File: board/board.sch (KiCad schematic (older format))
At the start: 12 parts, among them J1 MOTION DETECTOR, J2 EXT BUTTON, U1 APA102 (RGB), U2 APA102 (W)

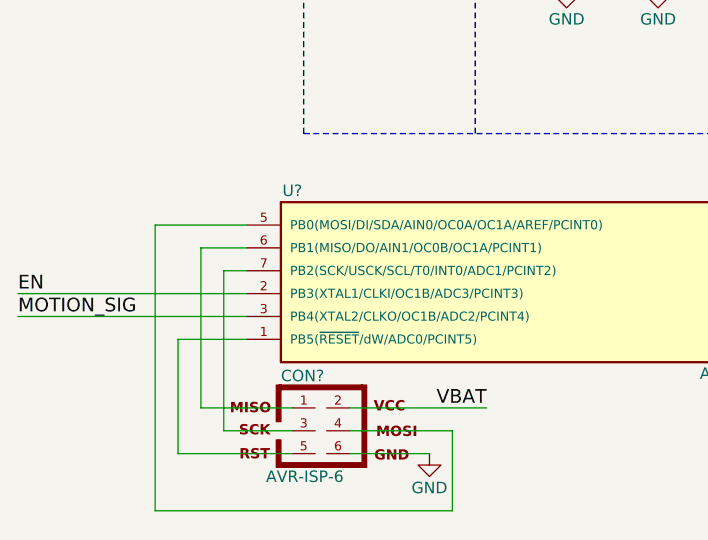
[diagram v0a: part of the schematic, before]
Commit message: Add attiny85 to control power
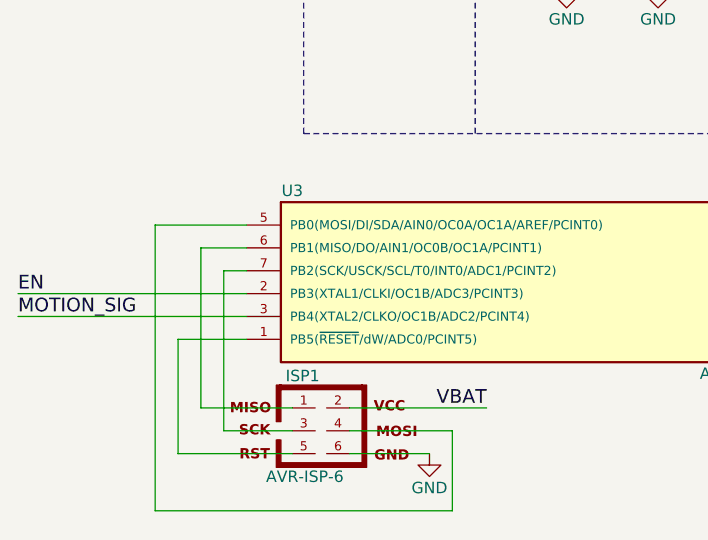
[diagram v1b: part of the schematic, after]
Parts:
- ISP1: renamed from CON?; footprint AVR-ISP-6 -> Pin_Headers:Pin_Header_Straight_2x03_Pitch2.54mm
- J1: footprint Pin_Headers:Pin_Header_Straight_1x03_Pitch2.54mm -> Pin_Headers:Pin_Header_Angled_1x03_Pitch2.54mm
- J2: footprint Pin_Headers:Pin_Header_Straight_1x02_Pitch2.54mm -> Pin_Headers:Pin_Header_Angled_1x02_Pitch2.54mm
- R1, R2, R4: footprint Discret:R3 -> Resistors_SMD:R_0805_HandSoldering
- U3: renamed from U?; footprint Housings_DIP:DIP-8_W7.62mm -> Housings_SOIC:SOIC-8_3.9x4.9mm_Pitch1.27mm
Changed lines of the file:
@@
 Adafruit FeatherWing\n
 $Comp
-L VCC #PWR8
+L VCC #PWR01
 U 1 1 56D753B8
 P 9700 750
-F 0 "#PWR8" H 9700 600 50  0001 C CNN
+F 0 "#PWR01" H 9700 600 50  0001 C CNN
 F 1 "VCC" H 9700 900 50  0000 C CNN
 F 2 "" H 9700 750 50  0000 C CNN
@@
 $EndComp
 $Comp
-L GND #PWR9
+L GND #PWR02
 U 1 1 56D75A03
 P 9700 2500
-F 0 "#PWR9" H 9700 2250 50  0001 C CNN
+F 0 "#PWR02" H 9700 2250 50  0001 C CNN
 F 1 "GND" H 9700 2350 50  0000 C CNN
 F 2 "" H 9700 2500 50  0000 C CNN
@@
 NoConn ~ 10050 2400
 $Comp
-L GND #PWR6
+L GND #PWR03
 U 1 1 59796D2F
 P 7800 3800
-F 0 "#PWR6" H 7800 3550 50  0001 C CNN
+F 0 "#PWR03" H 7800 3550 50  0001 C CNN
 F 1 "GND" H 7800 3650 50  0000 C CNN
 F 2 "" H 7800 3800 50  0001 C CNN
@@
 F 0 "J1" H 7400 1150 50  0000 C CNN
 F 1 "MOTION DETECTOR" V 7500 950 50  0000 C CNN
-F 2 "Pin_Headers:Pin_Header_Straight_1x03_Pitch2.54mm" H 7400 950 50  0001 C CNN
+F 2 "Pin_Headers:Pin_Header_Angled_1x03_Pitch2.54mm" H 7400 950 50  0001 C CNN
 F 3 "" H 7400 950 50  0001 C CNN
 	1    7400 950
@@
 F 0 "R1" V 5700 1200 50  0000 C CNN
 F 1 "22.6K" V 5800 1200 39  0000 C CNN
-F 2 "Discret:R3" V 5730 1200 50  0001 C CNN
+F 2 "Resistors_SMD:R_0805_HandSoldering" V 5730 1200 50  0001 C CNN
 F 3 "" H 5800 1200 50  0001 C CNN
 	1    5800 1200
@@
 F 0 "R2" V 5880 1950 50  0000 C CNN
 F 1 "10K" V 5800 1950 50  0000 C CNN
-F 2 "Discret:R3" V 5730 1950 50  0001 C CNN
+F 2 "Resistors_SMD:R_0805_HandSoldering" V 5730 1950 50  0001 C CNN
 F 3 "" H 5800 1950 50  0001 C CNN
 	1    5800 1950
@@
 Connection ~ 5800 1400
 $Comp
-L GND #PWR3
+L GND #PWR04
 U 1 1 597CE63C
 P 5800 2100
-F 0 "#PWR3" H 5800 1850 50  0001 C CNN
+F 0 "#PWR04" H 5800 1850 50  0001 C CNN
 F 1 "GND" H 5800 1950 50  0000 C CNN
 F 2 "" H 5800 2100 50  0001 C CNN
@@
 $EndComp
 $Comp
-L VCC #PWR2
+L VCC #PWR05
 U 1 1 597CEF49
 P 5800 1050
-F 0 "#PWR2" H 5800 900 50  0001 C CNN
+F 0 "#PWR05" H 5800 900 50  0001 C CNN
 F 1 "VCC" H 5800 1200 50  0000 C CNN
 F 2 "" H 5800 1050 50  0001 C CNN
@@
 F 0 "R4" V 6280 1950 50  0000 C CNN
 F 1 "10K" V 6200 1950 50  0000 C CNN
-F 2 "Discret:R3" V 6130 1950 50  0001 C CNN
+F 2 "Resistors_SMD:R_0805_HandSoldering" V 6130 1950 50  0001 C CNN
 F 3 "" H 6200 1950 50  0001 C CNN
 	1    6200 1950
@@
 $EndComp
 $Comp
-L GND #PWR4
+L GND #PWR06
 U 1 1 597D0A0F
 P 6200 2100
-F 0 "#PWR4" H 6200 1850 50  0001 C CNN
+F 0 "#PWR06" H 6200 1850 50  0001 C CNN
 F 1 "GND" H 6200 1950 50  0000 C CNN
 F 2 "" H 6200 2100 50  0001 C CNN
@@
 Connection ~ 6200 1750
 $Comp
-L GND #PWR7
+L GND #PWR07
 U 1 1 597D0EF3
 P 7950 2350
-F 0 "#PWR7" H 7950 2100 50  0001 C CNN
+F 0 "#PWR07" H 7950 2100 50  0001 C CNN
 F 1 "GND" H 7950 2200 50  0000 C CNN
 F 2 "" H 7950 2350 50  0001 C CNN
@@
 F 0 "J2" H 5000 1650 50  0000 C CNN
 F 1 "EXT BUTTON" V 5100 1500 50  0000 C CNN
-F 2 "Pin_Headers:Pin_Header_Straight_1x02_Pitch2.54mm" H 5000 1500 50  0001 C CNN
+F 2 "Pin_Headers:Pin_Header_Angled_1x02_Pitch2.54mm" H 5000 1500 50  0001 C CNN
 F 3 "" H 5000 1500 50  0001 C CNN
 	1    5000 1500
@@
 $EndComp
 $Comp
-L GND #PWR1
+L GND #PWR08
 U 1 1 597D2087
 P 5050 1900
-F 0 "#PWR1" H 5050 1650 50  0001 C CNN
+F 0 "#PWR08" H 5050 1650 50  0001 C CNN
 F 1 "GND" H 5050 1750 50  0000 C CNN
 F 2 "" H 5050 1900 50  0001 C CNN
@@
 	4650 2750 4650 500
 $Comp
-L ATTINY85-20PU U?
+L ATTINY85-20PU U3
 U 1 1 597D0F49
 P 5750 3400
-F 0 "U?" H 4600 3800 50  0000 C CNN
+F 0 "U3" H 4600 3800 50  0000 C CNN
 F 1 "ATTINY85-20PU" H 6650 3000 50  0000 C CNN
-F 2 "Housings_DIP:DIP-8_W7.62mm" H 6750 3400 50  0001 C CIN
+F 2 "Housings_SOIC:SOIC-8_3.9x4.9mm_Pitch1.27mm" H 6750 3400 50  0001 C CIN
 F 3 "" H 5750 3400 50  0001 C CNN
 	1    5750 3400
@@
 $EndComp
 $Comp
-L GND #PWR?
+L GND #PWR09
 U 1 1 597D1088
 P 7100 3650
-F 0 "#PWR?" H 7100 3400 50  0001 C CNN
+F 0 "#PWR09" H 7100 3400 50  0001 C CNN
 F 1 "GND" H 7100 3500 50  0000 C CNN
 F 2 "" H 7100 3650 50  0001 C CNN
@@
 $EndComp
 $Comp
-L AVR-ISP-6 CON?
+L AVR-ISP-6 ISP1
 U 1 1 597D1114
 P 4750 4050
-F 0 "CON?" H 4645 4290 50  0000 C CNN
+F 0 "ISP1" H 4645 4290 50  0000 C CNN
 F 1 "AVR-ISP-6" H 4485 3820 50  0000 L BNN
-F 2 "AVR-ISP-6" V 4230 4090 50  0001 C CNN
+F 2 "Pin_Headers:Pin_Header_Straight_2x03_Pitch2.54mm" V 4230 4090 50  0001 C CNN
 F 3 "" H 4725 4050 50  0001 C CNN
 	1    4750 4050
@@
 	4300 3350 4400 3350
 $Comp
-L GND #PWR?
+L GND #PWR010
 U 1 1 597D12FA
 P 5200 4150
-F 0 "#PWR?" H 5200 3900 50  0001 C CNN
+F 0 "#PWR010" H 5200 3900 50  0001 C CNN
 F 1 "GND" H 5200 4000 50  0000 C CNN
 F 2 "" H 5200 4150 50  0001 C CNN
@@
 	7800 2350 7800 1750
 $Comp
-L VCC #PWR?
+L VCC #PWR011
 U 1 1 597D3E37
 P 7800 1750
-F 0 "#PWR?" H 7800 1600 50  0001 C CNN
+F 0 "#PWR011" H 7800 1600 50  0001 C CNN
 F 1 "VCC" H 7800 1900 50  0000 C CNN
 F 2 "" H 7800 1750 50  0001 C CNN

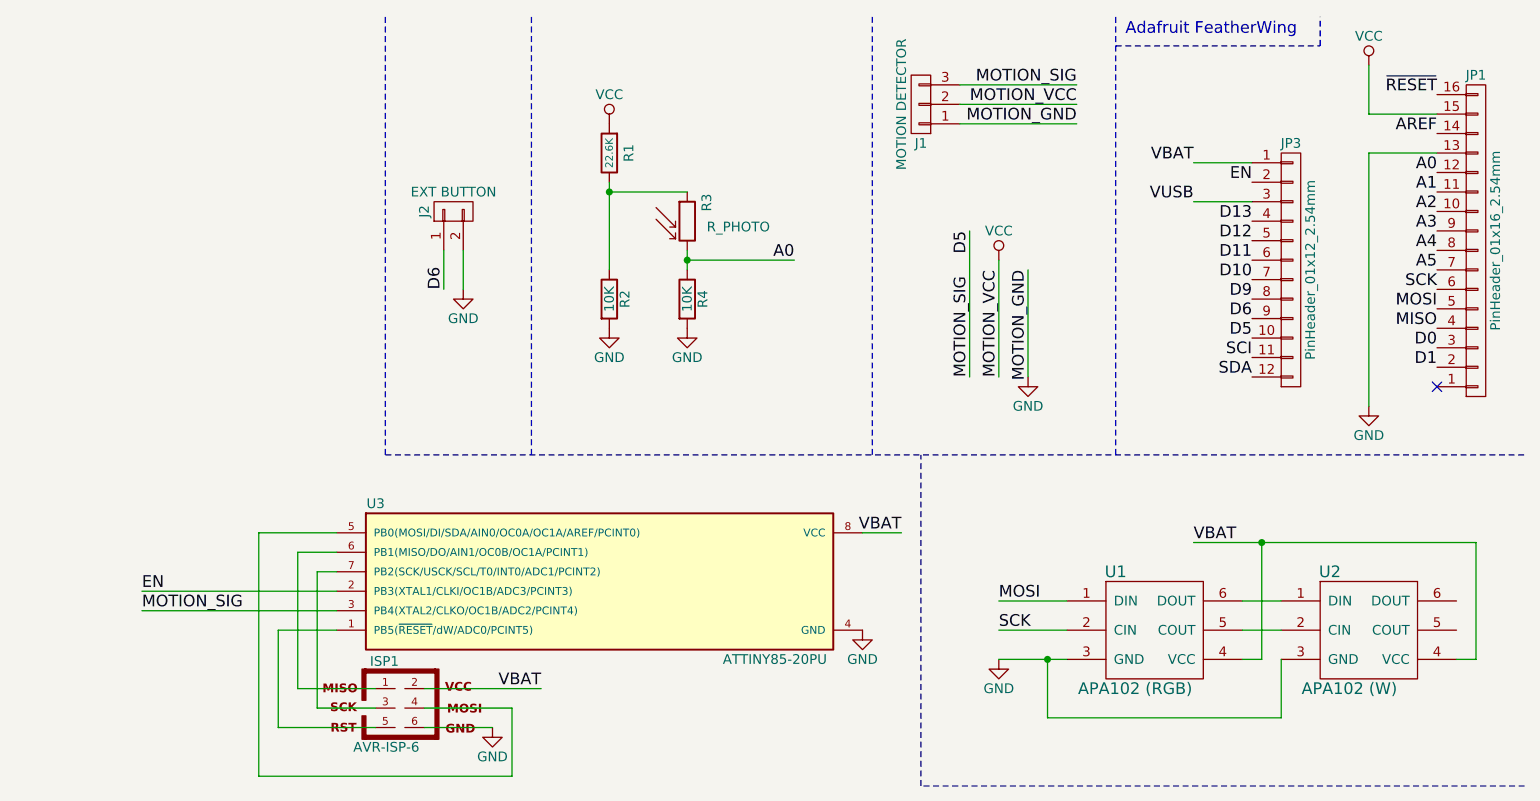
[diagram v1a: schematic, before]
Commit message: Add protection resistors
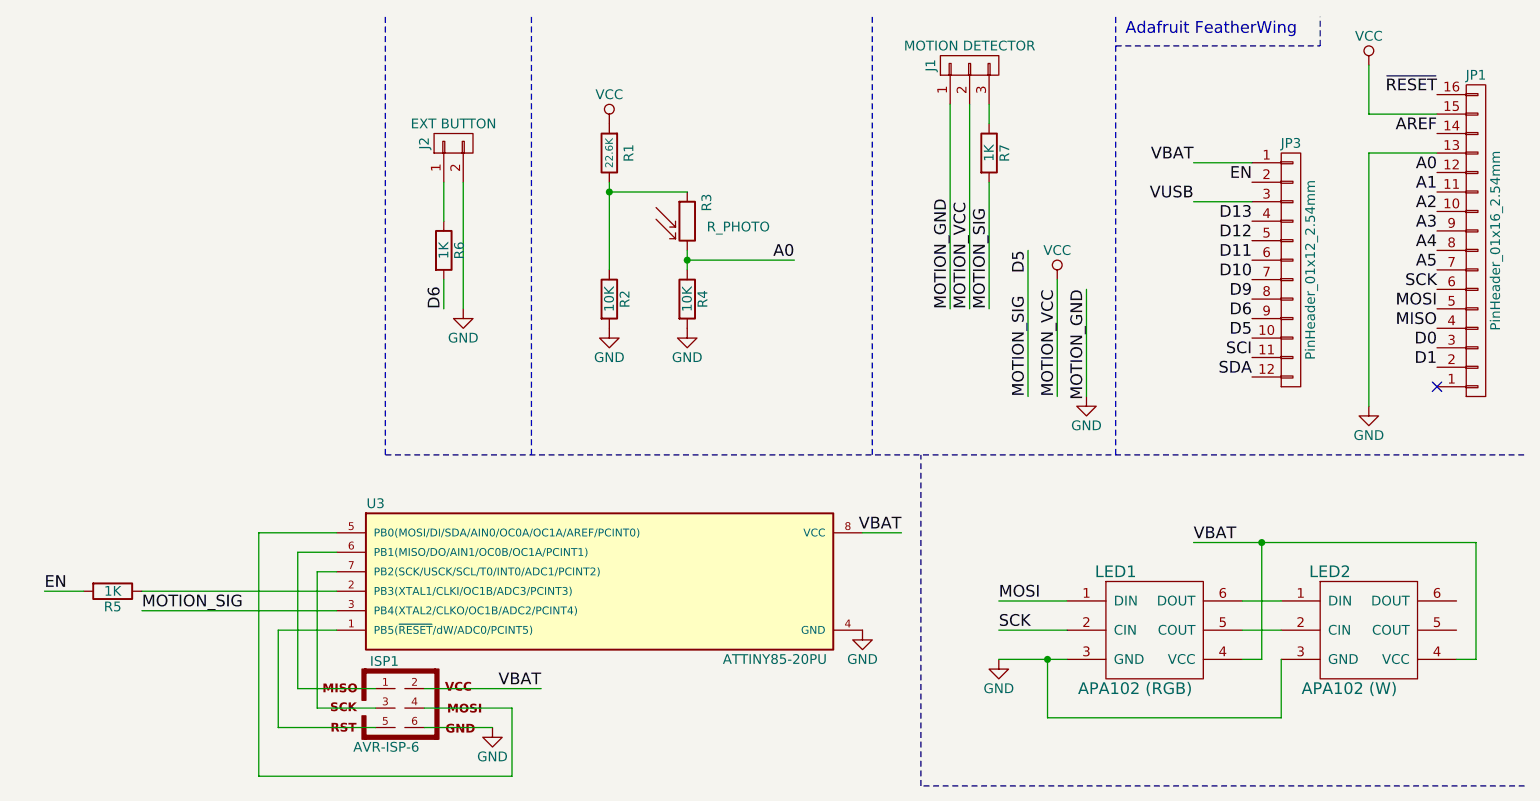
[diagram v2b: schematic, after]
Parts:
- added R5, R6, R7: 1K, Resistors_SMD:R_0805_HandSoldering, symbol R
- renumbered U1 to LED1, U2 to LED2
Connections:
- net D5: now also R7.2; no longer J1.3 (P3)
- net D6: now also R6.2; no longer J2.1 (P1)
- net EN: now also R5.2; no longer U3.2 (PB3(XTAL1/CLKI/OC1B/ADC3/PCINT3))
- new net: J1.3 (P3), R7.1
- new net: R5.1, U3.2 (PB3(XTAL1/CLKI/OC1B/ADC3/PCINT3))
- new net: J2.1 (P1), R6.1
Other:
- moved on the sheet: J1, J2
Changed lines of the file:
@@
 MOSI
 $Comp
-L APA102 U1
+L APA102 LED1
 U 1 1 59797576
 P 8600 3650
-F 0 "U1" H 8400 3950 60  0000 C CNN
+F 0 "LED1" H 8400 3950 60  0000 C CNN
 F 1 "APA102 (RGB)" H 8500 3350 60  0000 C CNN
 F 2 "CrumpPrints:APA102" H 8600 3200 60  0001 C CNN
@@
 	7800 3800 8150 3800
 $Comp
-L APA102 U2
+L APA102 LED2
 U 1 1 5979778F
 P 9700 3650
-F 0 "U2" H 9500 3950 60  0000 C CNN
+F 0 "LED2" H 9500 3950 60  0000 C CNN
 F 1 "APA102 (W)" H 9600 3350 60  0000 C CNN
 F 2 "CrumpPrints:APA102" H 9700 3200 60  0001 C CNN
@@
 L CONN_01X03 J1
 U 1 1 59797A62
-P 7400 950
-F 0 "J1" H 7400 1150 50  0000 C CNN
-F 1 "MOTION DETECTOR" V 7500 950 50  0000 C CNN
-F 2 "Pin_Headers:Pin_Header_Angled_1x03_Pitch2.54mm" H 7400 950 50  0001 C CNN
-F 3 "" H 7400 950 50  0001 C CNN
-	1    7400 950
-	-1   0    0    1
+P 7650 750
+F 0 "J1" H 7650 950 50  0000 C CNN
+F 1 "MOTION DETECTOR" V 7750 750 50  0000 C CNN
+F 2 "Pin_Headers:Pin_Header_Angled_1x03_Pitch2.54mm" H 7650 750 50  0001 C CNN
+F 3 "" H 7650 750 50  0001 C CNN
+	1    7650 750
+	0    -1   -1   0
 $EndComp
 $Comp
@@
 L GND #PWR07
 U 1 1 597D0EF3
-P 7950 2350
-F 0 "#PWR07" H 7950 2100 50  0001 C CNN
-F 1 "GND" H 7950 2200 50  0000 C CNN
-F 2 "" H 7950 2350 50  0001 C CNN
-F 3 "" H 7950 2350 50  0001 C CNN
-	1    7950 2350
-	1    0    0    -1
-$EndComp
-Wire Wire Line
-	7650 1600 7650 2350
-Text Label 7650 1600 3    60   ~ 0
+P 8250 2450
+F 0 "#PWR07" H 8250 2200 50  0001 C CNN
+F 1 "GND" H 8250 2300 50  0000 C CNN
+F 2 "" H 8250 2450 50  0001 C CNN
+F 3 "" H 8250 2450 50  0001 C CNN
+	1    8250 2450
+	1    0    0    -1
+$EndComp
+Wire Wire Line
+	7950 1700 7950 2450
+Text Label 7950 1700 3    60   ~ 0
 D5
 Wire Notes Line
@@
 L CONN_01X02 J2
 U 1 1 597D1FB0
-P 5000 1500
-F 0 "J2" H 5000 1650 50  0000 C CNN
-F 1 "EXT BUTTON" V 5100 1500 50  0000 C CNN
-F 2 "Pin_Headers:Pin_Header_Angled_1x02_Pitch2.54mm" H 5000 1500 50  0001 C CNN
-F 3 "" H 5000 1500 50  0001 C CNN
-	1    5000 1500
+P 5000 1150
+F 0 "J2" H 5000 1300 50  0000 C CNN
+F 1 "EXT BUTTON" V 5100 1150 50  0000 C CNN
+F 2 "Pin_Headers:Pin_Header_Angled_1x02_Pitch2.54mm" H 5000 1150 50  0001 C CNN
+F 3 "" H 5000 1150 50  0001 C CNN
+	1    5000 1150
 	0    -1   -1   0
 $EndComp
@@
 L GND #PWR08
 U 1 1 597D2087
-P 5050 1900
-F 0 "#PWR08" H 5050 1650 50  0001 C CNN
-F 1 "GND" H 5050 1750 50  0000 C CNN
-F 2 "" H 5050 1900 50  0001 C CNN
-F 3 "" H 5050 1900 50  0001 C CNN
-	1    5050 1900
-	1    0    0    -1
-$EndComp
-Wire Wire Line
-	5050 1700 5050 1900
-Wire Wire Line
-	4950 1700 4950 1900
-Text Label 4950 1900 1    60   ~ 0
+P 5050 2000
+F 0 "#PWR08" H 5050 1750 50  0001 C CNN
+F 1 "GND" H 5050 1850 50  0000 C CNN
+F 2 "" H 5050 2000 50  0001 C CNN
+F 3 "" H 5050 2000 50  0001 C CNN
+	1    5050 2000
+	1    0    0    -1
+$EndComp
+Wire Wire Line
+	5050 1350 5050 2000
+Wire Wire Line
+	4950 1350 4950 1550
+Text Label 4950 2000 1    60   ~ 0
 D6
 Wire Notes Line
@@
 Wire Wire Line
 	4400 3450 3400 3450
-Text Label 3400 3450 0    60   ~ 0
+Text Label 2900 3450 0    60   ~ 0
 EN
-Text Label 8200 1050 2    60   ~ 0
+Text Label 7550 2000 1    60   ~ 0
 MOTION_GND
 Wire Wire Line
-	8200 1050 7600 1050
-Wire Wire Line
-	8200 950  7600 950
-Wire Wire Line
-	8200 850  7600 850
-Text Label 8200 950  2    60   ~ 0
+	7550 2000 7550 950
+Wire Wire Line
+	7650 2000 7650 950
+Wire Wire Line
+	7750 1050 7750 950
+Text Label 7650 2000 1    60   ~ 0
 MOTION_VCC
-Text Label 8200 850  2    60   ~ 0
+Text Label 7750 2000 1    60   ~ 0
 MOTION_SIG
-Text Label 7800 2350 1    60   ~ 0
+Text Label 8100 2450 1    60   ~ 0
 MOTION_VCC
 Wire Wire Line
-	7800 2350 7800 1750
+	8100 2450 8100 1850
 $Comp
 L VCC #PWR011
 U 1 1 597D3E37
-P 7800 1750
-F 0 "#PWR011" H 7800 1600 50  0001 C CNN
-F 1 "VCC" H 7800 1900 50  0000 C CNN
-F 2 "" H 7800 1750 50  0001 C CNN
-F 3 "" H 7800 1750 50  0001 C CNN
-	1    7800 1750
-	1    0    0    -1
-$EndComp
-Wire Wire Line
-	7950 1800 7950 2350
-Text Label 7950 1800 3    60   ~ 0
+P 8100 1850
+F 0 "#PWR011" H 8100 1700 50  0001 C CNN
+F 1 "VCC" H 8100 2000 50  0000 C CNN
+F 2 "" H 8100 1850 50  0001 C CNN
+F 3 "" H 8100 1850 50  0001 C CNN
+	1    8100 1850
+	1    0    0    -1
+$EndComp
+Wire Wire Line
+	8250 1900 8250 2450
+Text Label 8250 1900 3    60   ~ 0
 MOTION_GND
-Text Label 7650 2350 1    60   ~ 0
+Text Label 7950 2450 1    60   ~ 0
 MOTION_SIG
 Text Label 3400 3550 0    60   ~ 0
@@
 Text Label 5450 3950 2    60   ~ 0
 VBAT
+$Comp
+L R R5
+U 1 1 5982A455
+P 3250 3450
+F 0 "R5" V 3330 3450 50  0000 C CNN
+F 1 "1K" V 3250 3450 50  0000 C CNN
+F 2 "Resistors_SMD:R_0805_HandSoldering" V 3180 3450 50  0001 C CNN
+F 3 "" H 3250 3450 50  0001 C CNN
+	1    3250 3450
+	0    1    1    0
+$EndComp
+Wire Wire Line
+	3100 3450 2900 3450
+$Comp
+L R R6
+U 1 1 5982A5C8
+P 4950 1700
+F 0 "R6" V 5030 1700 50  0000 C CNN
+F 1 "1K" V 4950 1700 50  0000 C CNN
+F 2 "Resistors_SMD:R_0805_HandSoldering" V 4880 1700 50  0001 C CNN
+F 3 "" H 4950 1700 50  0001 C CNN
+	1    4950 1700
+	1    0    0    -1
+$EndComp
+Wire Wire Line
+	4950 1850 4950 2000
+$Comp
+L R R7
+U 1 1 5982A87C
+P 7750 1200
+F 0 "R7" V 7830 1200 50  0000 C CNN
+F 1 "1K" V 7750 1200 50  0000 C CNN
+F 2 "Resistors_SMD:R_0805_HandSoldering" V 7680 1200 50  0001 C CNN
+F 3 "" H 7750 1200 50  0001 C CNN
+	1    7750 1200
+	1    0    0    -1
+$EndComp
+Wire Wire Line
+	7750 2000 7750 1350
 $EndSCHEMATC

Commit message: Rework
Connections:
- net EN: no longer R5.2
- net VBAT: no longer ISP1.2, U3.8 (VCC)
- net VCC: now also ISP1.2, U3.8 (VCC)
- net ~RESET: now also R5.2
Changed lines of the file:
@@
 L GND #PWR03
 U 1 1 59796D2F
-P 7800 3800
-F 0 "#PWR03" H 7800 3550 50  0001 C CNN
-F 1 "GND" H 7800 3650 50  0000 C CNN
-F 2 "" H 7800 3800 50  0001 C CNN
-F 3 "" H 7800 3800 50  0001 C CNN
-	1    7800 3800
+P 8150 3800
+F 0 "#PWR03" H 8150 3550 50  0001 C CNN
+F 1 "GND" H 8150 3650 50  0000 C CNN
+F 2 "" H 8150 3800 50  0001 C CNN
+F 3 "" H 8150 3800 50  0001 C CNN
+	1    8150 3800
 	1    0    0    -1
 $EndComp
@@
 P 8600 3650
 F 0 "LED1" H 8400 3950 60  0000 C CNN
-F 1 "APA102 (RGB)" H 8500 3350 60  0000 C CNN
+F 1 "APA102 (RGB)" H 8650 3350 60  0000 C CNN
 F 2 "CrumpPrints:APA102" H 8600 3200 60  0001 C CNN
 F 3 "" H 8600 3200 60  0000 C CNN
@@
 Wire Wire Line
 	7800 3500 8150 3500
-Wire Wire Line
-	7800 3800 8150 3800
 $Comp
 L APA102 LED2
@@
 P 9700 3650
 F 0 "LED2" H 9500 3950 60  0000 C CNN
-F 1 "APA102 (W)" H 9600 3350 60  0000 C CNN
+F 1 "APA102 (W)" H 9700 3350 60  0000 C CNN
 F 2 "CrumpPrints:APA102" H 9700 3200 60  0001 C CNN
 F 3 "" H 9700 3200 60  0000 C CNN
@@
 	1    0    0    -1
 $EndComp
-Wire Wire Line
-	8050 3800 8050 4100
-Wire Wire Line
-	8050 4100 9250 4100
-Wire Wire Line
-	9250 4100 9250 3800
-Connection ~ 8050 3800
 Wire Wire Line
 	9050 3800 9150 3800
@@
 Wire Wire Line
 	4400 3450 3400 3450
-Text Label 2900 3450 0    60   ~ 0
-EN
+Text Label 2800 3450 0    60   ~ 0
+~RESET
 Text Label 7550 2000 1    60   ~ 0
 MOTION_GND
@@
 	7100 3150 7300 3150
 Text Label 7300 3150 2    60   ~ 0
-VBAT
+VCC
 Text Label 5450 3950 2    60   ~ 0
-VBAT
+VCC
 $Comp
 L R R5
@@
 $EndComp
 Wire Wire Line
-	3100 3450 2900 3450
+	3100 3450 2800 3450
 $Comp
 L R R6
@@
 Wire Wire Line
 	7750 2000 7750 1350
+$Comp
+L GND #PWR012
+U 1 1 5986A206
+P 9250 3800
+F 0 "#PWR012" H 9250 3550 50  0001 C CNN
+F 1 "GND" H 9250 3650 50  0000 C CNN
+F 2 "" H 9250 3800 50  0001 C CNN
+F 3 "" H 9250 3800 50  0001 C CNN
+	1    9250 3800
+	1    0    0    -1
+$EndComp
 $EndSCHEMATC

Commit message: Move ISP header further from LEDs to prevent shadows
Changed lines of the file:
@@
 Text Label 3400 3550 0    60   ~ 0
 MOTION_SIG
-Wire Wire Line
-	7100 3150 7300 3150
-Text Label 7300 3150 2    60   ~ 0
-VCC
 Text Label 5450 3950 2    60   ~ 0
 VCC
@@
 	1    0    0    -1
 $EndComp
+$Comp
+L VCC #PWR?
+U 1 1 5987EE9E
+P 7100 3150
+F 0 "#PWR?" H 7100 3000 50  0001 C CNN
+F 1 "VCC" H 7100 3300 50  0000 C CNN
+F 2 "" H 7100 3150 50  0001 C CNN
+F 3 "" H 7100 3150 50  0001 C CNN
+	1    7100 3150
+	1    0    0    -1
+$EndComp
